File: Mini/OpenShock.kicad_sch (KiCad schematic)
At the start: 41 parts, among them J1 USB_C_Receptacle_USB2.0, J2 Conn_01x03, J3 Conn_01x03, J4 Conn_01x06, J6 Conn_01x04, SW1 KH-6X6X6H-TJ, SW2 KH-6X6X6H-TJ, SW3 KH-6X6X6H-TJ, U1 ESP32-S3-WROOM-1, U2 AMS1117-3.3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

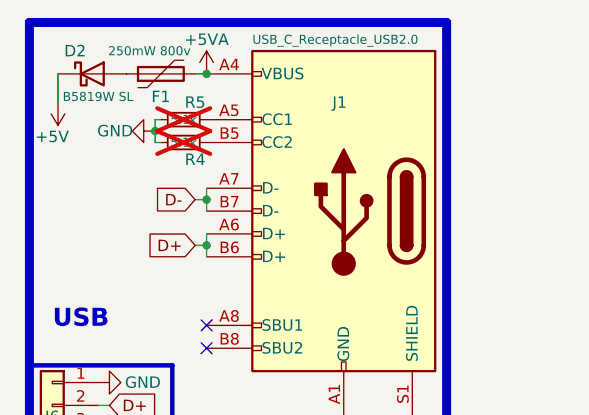
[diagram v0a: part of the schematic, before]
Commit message: Schematic Fixes + Add BoM
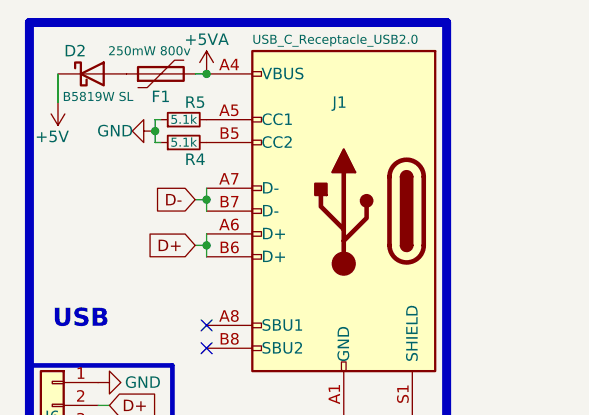
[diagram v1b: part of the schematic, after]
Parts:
- R4, R5: now fitted
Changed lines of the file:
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@@
 		(in_bom yes)
 		(on_board yes)
-		(dnp yes)
+		(dnp no)
 		(property "Reference" "R4"
 			(at 31.75 45.72 90)
@@
 		(in_bom yes)
 		(on_board yes)
-		(dnp yes)
+		(dnp no)
 		(property "Reference" "R5"
 			(at 31.75 39.37 90)

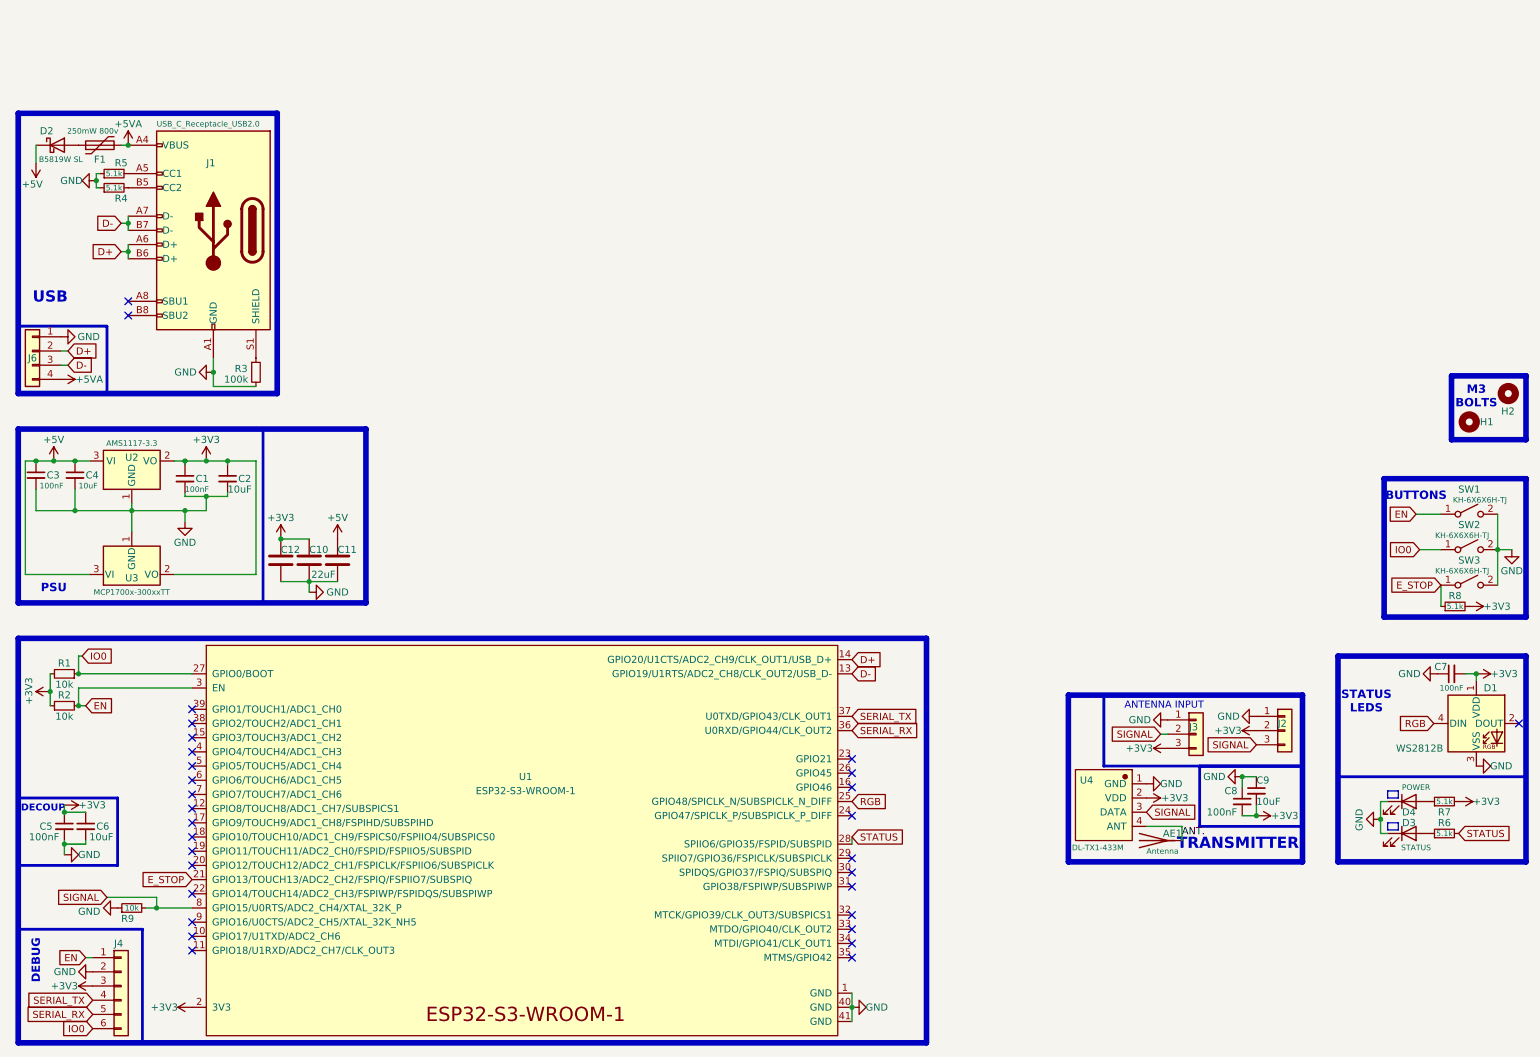
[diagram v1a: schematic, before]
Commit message: R1.1; Upgrade from AMS1117 to Low-Noise TI chip; TPS7A2033PDBVR, 300mA output
Added locally saved images of board, rather than Github cache.
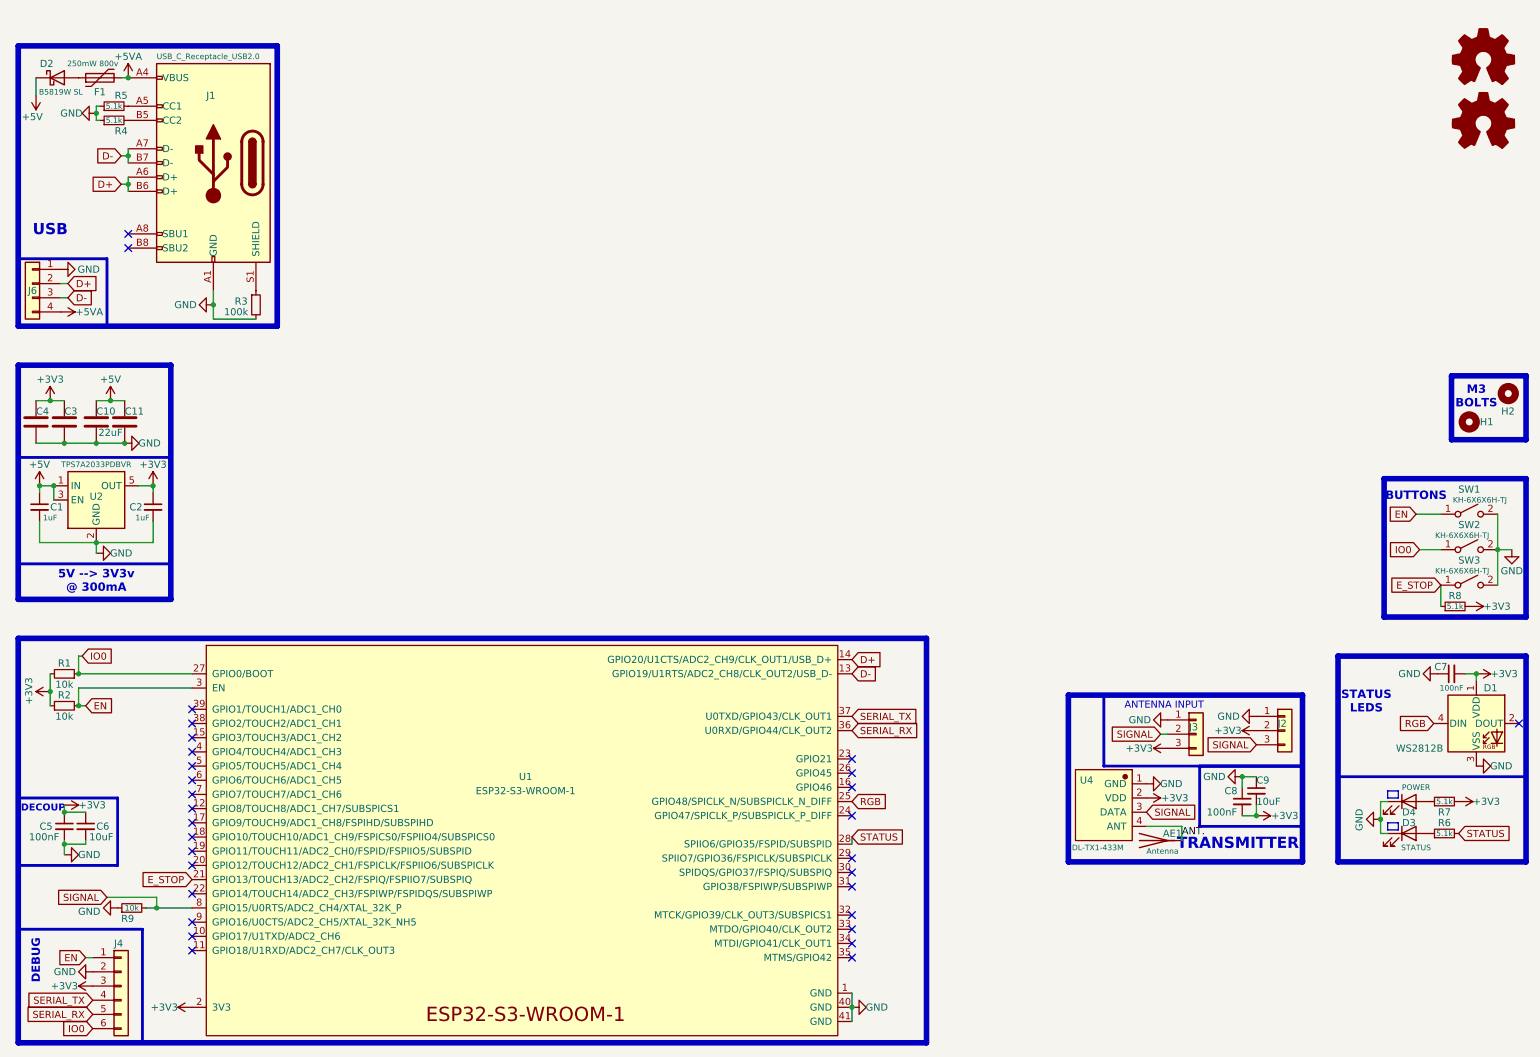
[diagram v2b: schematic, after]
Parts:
- removed C12: 22uF, Capacitor_SMD:C_0603_1608Metric_Pad1.08x0.95mm_HandSolder, symbol Device:C
- removed C3: 100nF, Capacitor_SMD:C_0603_1608Metric_Pad1.08x0.95mm_HandSolder, symbol Device:C_Small
- removed C4: 10uF, Capacitor_SMD:C_0603_1608Metric_Pad1.08x0.95mm_HandSolder, symbol Device:C_Small
- removed U2: AMS1117-3.3, Package_TO_SOT_SMD:SOT-223-3_TabPin2, symbol Regulator_Linear:AMS1117-3.3
- removed U3: MCP1700x-300xxTT, Package_TO_SOT_SMD:SOT-23_Handsoldering, symbol Regulator_Linear:MCP1700x-300xxTT
- added C3, C4: 22uF, Capacitor_SMD:C_0603_1608Metric_Pad1.08x0.95mm_HandSolder, symbol Device:C
- added U2: TPS7A2033PDBVR, PCM_Package_TO_SOT_SMD_AKL:SOT-23-5_HandSoldering, symbol Regulator_Linear:TPS7A0508PDBV
- C1: value 100nF -> 1uF; LCSC C6119861 -> C5189821
- C2: value 10uF -> 1uF; LCSC C380316 -> C5189821
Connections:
- net +3V3: now also C3.1, C4.1, U2.5 (OUT); no longer C1.1, C10.1
- net +5V: now also C1.1, C10.1, U2.1 (IN), U2.3 (EN)
- net GND: now also C3.2, C4.2, U2.2 (GND)
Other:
- note added: "5V --> 3V3v @ 300mA"
- note removed: "PSU"
- moved on the sheet: D2, F1, J1, J6, R3, R4, R5

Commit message: New revision; Board fixes
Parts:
- added J5: Conn_01x02, Connector_PinHeader_2.54mm:PinHeader_1x02_P2.54mm_Vertical, symbol Connector_Generic:Conn_01x02
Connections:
- net at R7.1: now also J5.2 (Pin_2); no longer D4.2 (A)
- new net: D4.2 (A), J5.1 (Pin_1)
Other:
- moved on the sheet: C7, D1

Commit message: New Revision.
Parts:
- removed C11, C3: 22uF, Capacitor_SMD:C_0603_1608Metric_Pad1.08x0.95mm_HandSolder, symbol Device:C
- removed J5: Conn_01x02, Connector_PinHeader_2.54mm:PinHeader_1x02_P2.54mm_Vertical, symbol Connector_Generic:Conn_01x02
- removed U1: ESP32-S3-WROOM-1, RF_Module:ESP32-S3-WROOM-1, symbol Espressif:ESP32-S3-WROOM-1
- removed U2: TPS7A2033PDBVR, PCM_Package_TO_SOT_SMD_AKL:SOT-23-5_HandSoldering, symbol Regulator_Linear:TPS7A0508PDBV
- added CN1: PJ-3200, EASYEDA Footprints:AUDIO-TH_PJ-3200, symbol EASYEDA Symbols:PJ-3200
- added H3: MountingHole, MountingHole:MountingHole_3.2mm_M3_ISO7380, symbol Mechanical:MountingHole
- added J5: USB_B_Mini, EASYEDA Footprints:MICRO-USB-TH_UX-150-ARG4, symbol Connector:USB_B_Mini
- added JP1, JP2: SolderJumper_2_Open, Jumper:SolderJumper-2_P1.3mm_Bridged_RoundedPad1.0x1.5mm, symbol Jumper:SolderJumper_2_Bridged
- added TP1, TP2, TP3, TP4, TP5, TP6, TP7, TP8, TP9: TestPoint, TestPoint:TestPoint_Pad_D1.5mm, symbol Connector:TestPoint
- added U1: ESP32-S3-WROOM-1, CustomFootprints:ESP32-S3-WROOM-1, symbol RF_Module:ESP32-S3-WROOM-1
- added U2: AMS1117-3.3, Package_TO_SOT_SMD:SOT-89-3_Handsoldering, symbol Regulator_Linear:AMS1117-3.3
- AE1: Alt. (none) -> https://aliexpress.com/item/1005005557947265.html
- C1, C2: footprint Capacitor_SMD:C_0603_1608Metric_Pad1.08x0.95mm_HandSolder -> Capacitor_SMD:C_0805_2012Metric_Pad1.18x1.45mm_HandSolder; LCSC C5189821 -> C215803
- C10, C4: footprint Capacitor_SMD:C_0603_1608Metric_Pad1.08x0.95mm_HandSolder -> Capacitor_SMD:C_0805_2012Metric_Pad1.18x1.45mm_HandSolder; LCSC C7432770 -> C98190
- C5, C7, C8: footprint Capacitor_SMD:C_0603_1608Metric_Pad1.08x0.95mm_HandSolder -> Capacitor_SMD:C_0805_2012Metric_Pad1.18x1.45mm_HandSolder; LCSC C6119861 -> C476766
- C6, C9: footprint Capacitor_SMD:C_0603_1608Metric_Pad1.08x0.95mm_HandSolder -> Capacitor_SMD:C_0805_2012Metric_Pad1.18x1.45mm_HandSolder; LCSC C380316 -> C1713
- R6: value 5.1k -> 10k
- U4: SuppliersPartNumber C381160 -> (none); uuid std:a9d6032d7d124c34850e850e6d051323 -> (none)
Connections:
- net +3V3: now also TP2.1, U1.2 (3V3), U2.2 (VO)
- net +5V: now also TP3.1, U2.3 (VI)
- net +5VA: now also J5.1 (VBUS), TP9.1
- net D+: now also J5.3 (D+), TP6.1, U1.14 (IO20)
- net D-: now also J5.2 (D-), TP7.1, U1.13 (IO19)
- net EN: now also U1.3 (EN)
- net E_STOP: now also CN1.4, U1.21 (IO13)
- net GND: now also J5.5 (GND), JP1.2 (B), JP2.2 (B), TP1.1, TP8.1, U1.1 (GND), U1.40 (GND), U1.41 (GND), U2.1 (GND)
- net IO0: now also U1.27 (IO0)
- net RGB: now also U1.25 (IO48)
- net SERIAL_RX: now also U1.36 (RXD0)
- net SERIAL_TX: now also U1.37 (TXD0)
- net SIGNAL: now also U1.8 (IO15)
- net STATUS: now also U1.28 (IO35)
- net at R7.1: now also D4.2 (A)
- net CC2: now reaches J1.B5 (CC2), R4.2
- net CC2: now also TP5.1
- net CC1: now reaches J1.A5 (CC1), R5.2
- net CC1: now also TP4.1
- net at J1.S1 (SHIELD), R3.1: now also J5.6 (Shield)
- new net: CN1.2, JP2.1 (A)
- new net: CN1.3, JP1.1 (A)
- no-connect marks 30 -> 31
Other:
- note added: "5V --> 3V3v @ 1A"
- note added: "E. STOP"
- note removed: "5V --> 3V3v @ 300mA"
- moved on the sheet: AE1, C1, C10, C2, C4, C5, C6, C7, C8, C9, D1, D2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
